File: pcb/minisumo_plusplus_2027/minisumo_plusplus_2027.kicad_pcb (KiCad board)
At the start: 2 copper layers, 211.1 x 112.8 mm, 9 parts, among them J3 Start Module - Conn_01x04_Pin, J5 Conn_01x10_Pin, SW1 SW_SPDT, U3 ESP32-C6-SuperMini

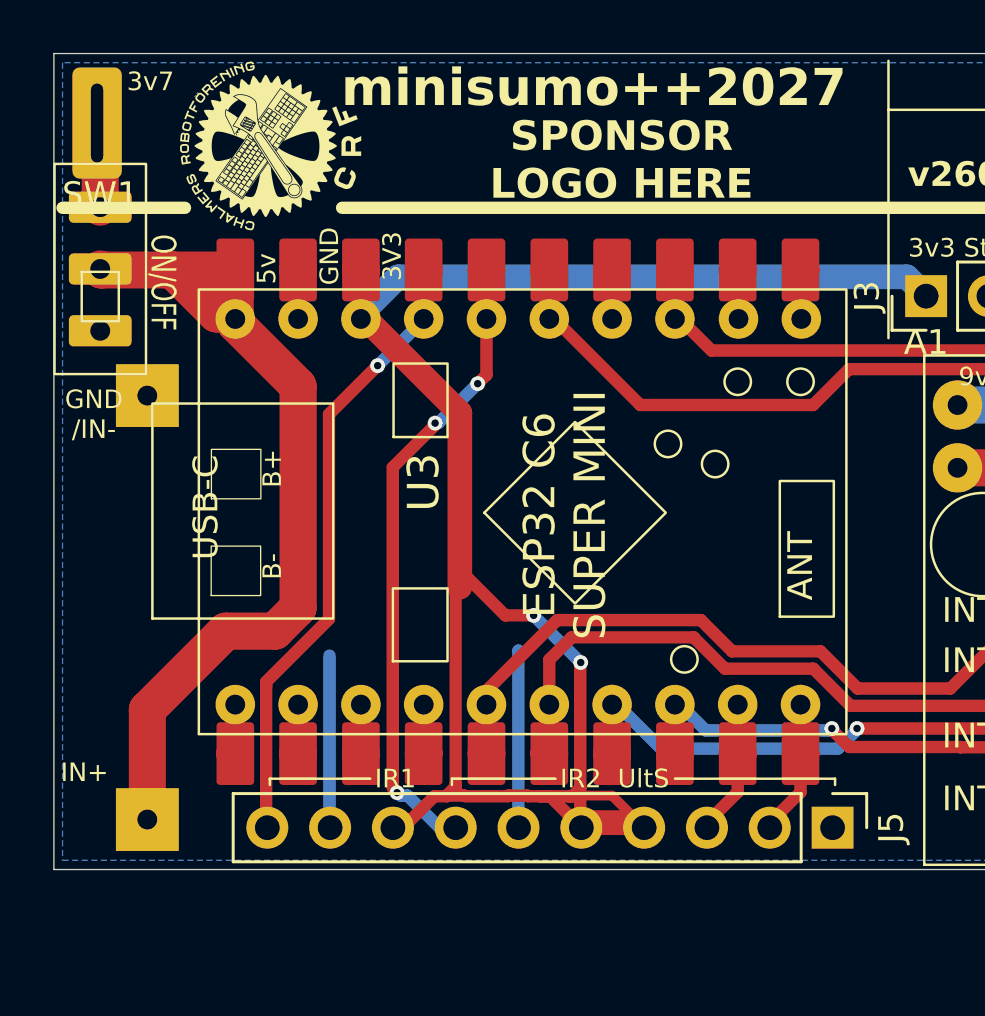
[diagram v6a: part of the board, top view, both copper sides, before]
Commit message: pcb refreshed ground plane
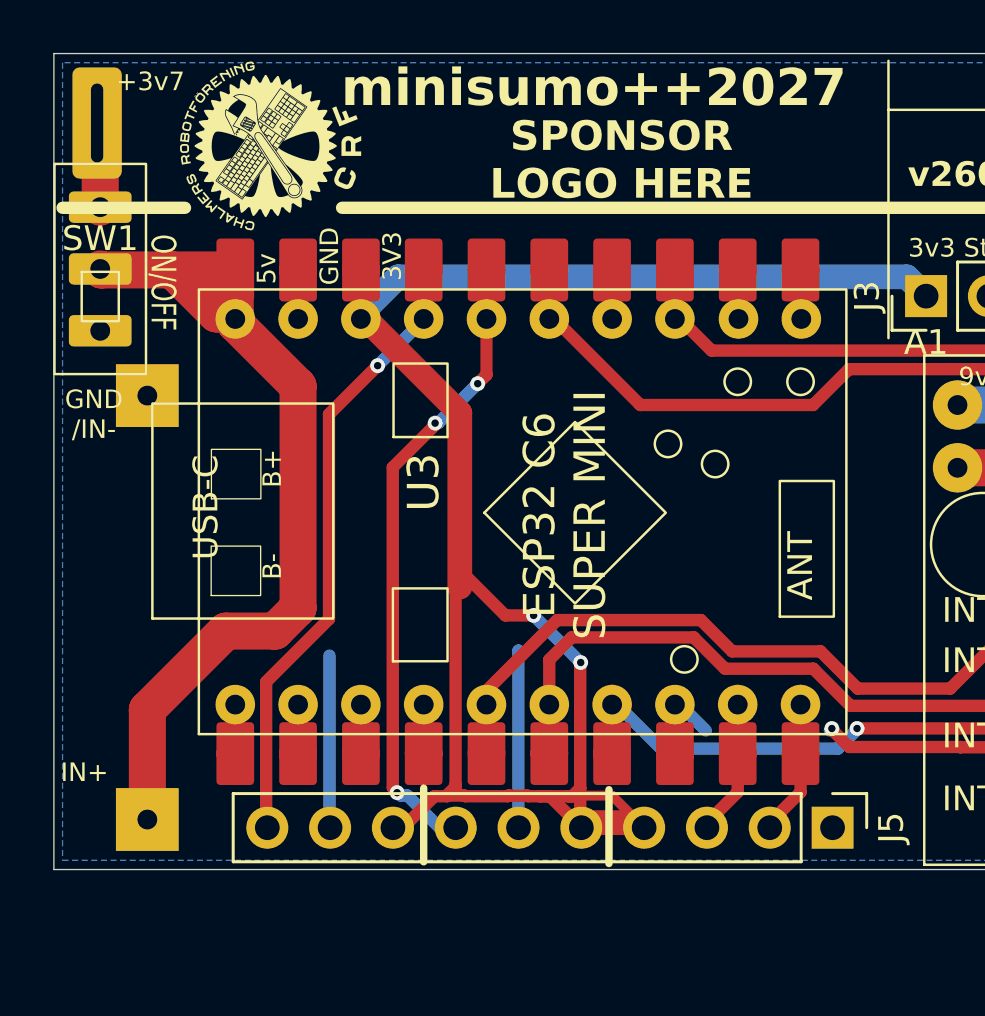
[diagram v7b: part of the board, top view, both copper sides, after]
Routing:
- net Net-(A1-INT4): track 18.6 -> 13.5 mm
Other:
- board text added: "+3v7"
- board text added: "3v3"
- board text removed: "3v7"

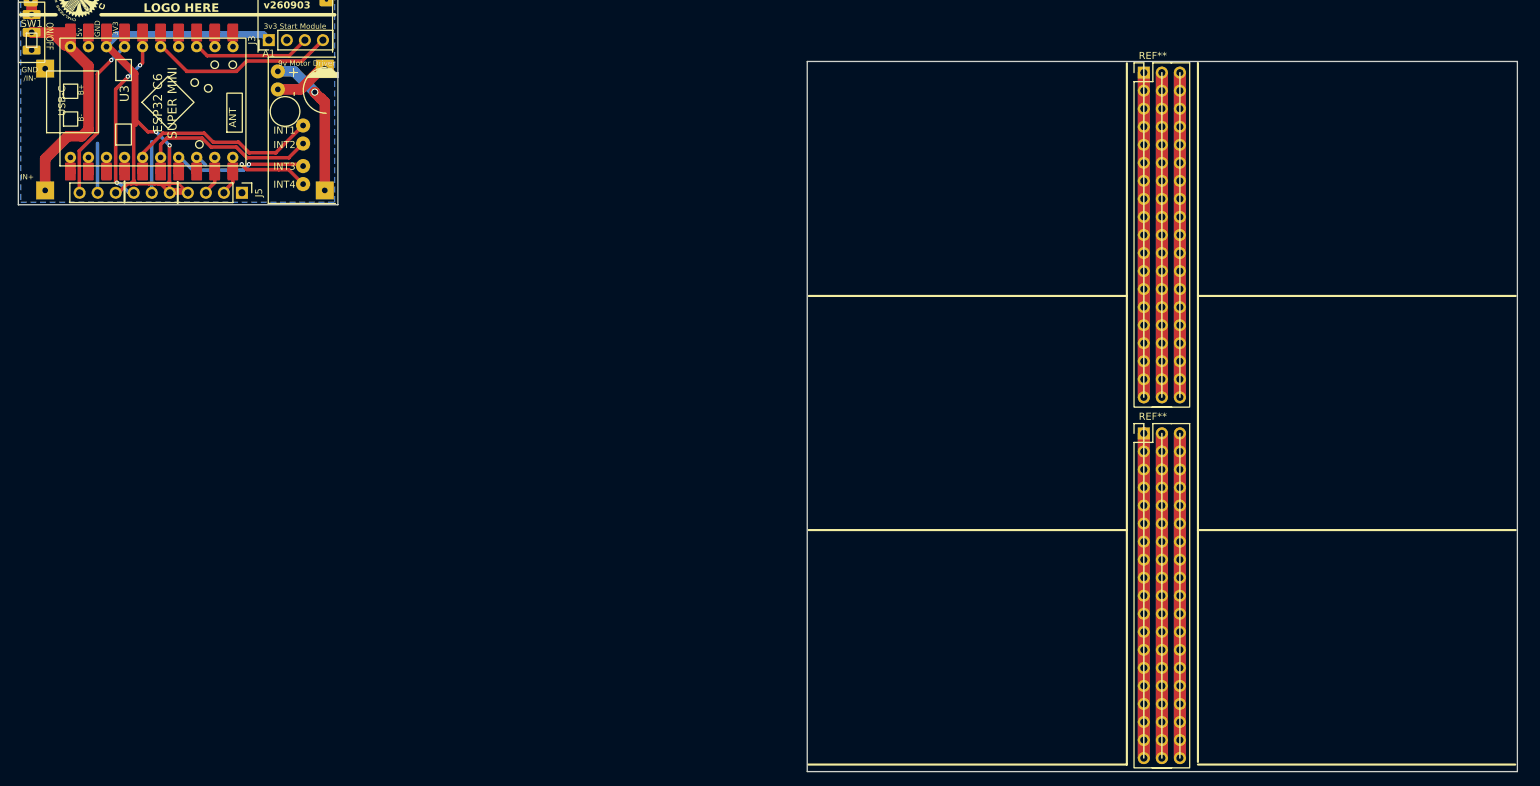
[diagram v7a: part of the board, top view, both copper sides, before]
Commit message: pcb latest w/ clean cutout and gerber (6x in 10x10cm)
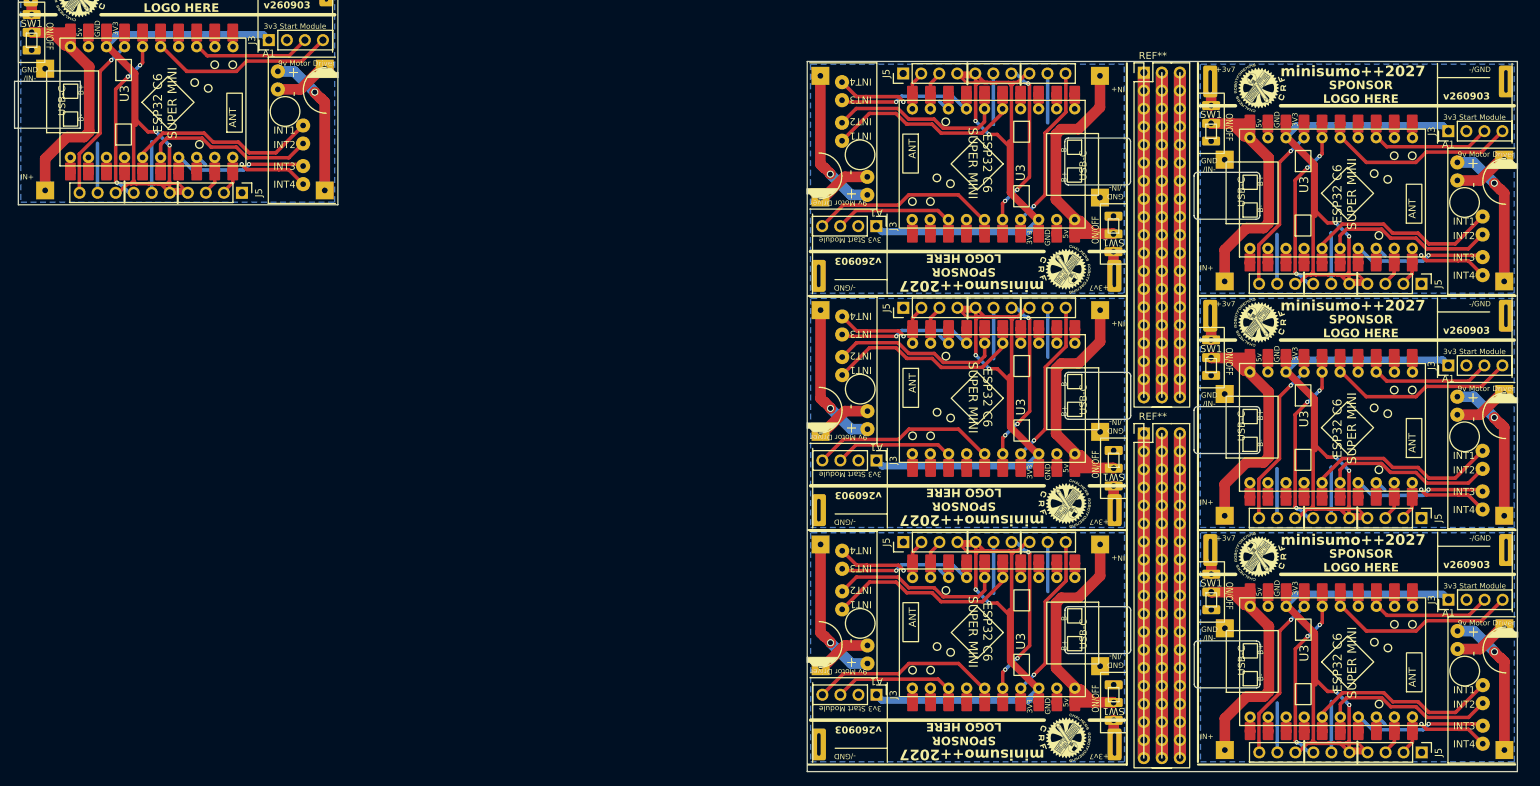
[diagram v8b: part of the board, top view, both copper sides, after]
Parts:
- added A1: ~, minisumo_plusplus_2027:Mini_L298N_2_Channel_H_Bridge_DC_Motor_Driver_Board_with_MX1508-special_silk, F.Cu at (149.7, 101.8)
- added A1: ~, minisumo_plusplus_2027:Mini_L298N_2_Channel_H_Bridge_DC_Motor_Driver_Board_with_MX1508-special_silk, F.Cu at (230.3, 126.2)
- added A1: ~, minisumo_plusplus_2027:Mini_L298N_2_Channel_H_Bridge_DC_Motor_Driver_Board_with_MX1508-special_silk, F.Cu at (230.2, 93.2)
- added A1: ~, minisumo_plusplus_2027:Mini_L298N_2_Channel_H_Bridge_DC_Motor_Driver_Board_with_MX1508-special_silk, F.Cu at (149.7, 68.8)
- added A1: ~, minisumo_plusplus_2027:Mini_L298N_2_Channel_H_Bridge_DC_Motor_Driver_Board_with_MX1508-special_silk, F.Cu at (230.2, 60.2)
- added A1: ~, minisumo_plusplus_2027:Mini_L298N_2_Channel_H_Bridge_DC_Motor_Driver_Board_with_MX1508-special_silk, F.Cu at (149.7, 134.8)
- added A2: ~, minisumo_plusplus_2027:XL6009 4A Boost Converter Step Up Adjustable 15W 5-32V to 5-50V DC-DC Power Supply Module LM2577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, B.Cu at (183.1, 114.1)
- added A2: ~, minisumo_plusplus_2027:XL6009 4A Boost Converter Step Up Adjustable 15W 5-32V to 5-50V DC-DC Power Supply Module LM2577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, B.Cu at (183.1, 48.1)
- added A2: ~, minisumo_plusplus_2027:XL6009 4A Boost Converter Step Up Adjustable 15W 5-32V to 5-50V DC-DC Power Supply Module LM2577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, B.Cu at (196.8, 80.9)
- added A2: ~, minisumo_plusplus_2027:XL6009 4A Boost Converter Step Up Adjustable 15W 5-32V to 5-50V DC-DC Power Supply Module LM2577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, B.Cu at (196.9, 146.9)
- added A2: ~, minisumo_plusplus_2027:XL6009 4A Boost Converter Step Up Adjustable 15W 5-32V to 5-50V DC-DC Power Supply Module LM2577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, B.Cu at (183.1, 81.1)
- added A2: ~, minisumo_plusplus_2027:XL6009 4A Boost Converter Step Up Adjustable 15W 5-32V to 5-50V DC-DC Power Supply Module LM2577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, B.Cu at (196.8, 113.9)
- added J3: Start Module - Conn_01x04_Pin, Connector_PinHeader_2.54mm:PinHeader_1x04_P2.54mm_Vertical, F.Cu at (230.3, 123.8)
- added J3: Start Module - Conn_01x04_Pin, Connector_PinHeader_2.54mm:PinHeader_1x04_P2.54mm_Vertical, F.Cu at (149.7, 137.2)
- added J3: Start Module - Conn_01x04_Pin, Connector_PinHeader_2.54mm:PinHeader_1x04_P2.54mm_Vertical, F.Cu at (230.2, 57.8)
- added J3: Start Module - Conn_01x04_Pin, Connector_PinHeader_2.54mm:PinHeader_1x04_P2.54mm_Vertical, F.Cu at (149.7, 71.2)
- added J3: Start Module - Conn_01x04_Pin, Connector_PinHeader_2.54mm:PinHeader_1x04_P2.54mm_Vertical, F.Cu at (149.7, 104.2)
- added J3: Start Module - Conn_01x04_Pin, Connector_PinHeader_2.54mm:PinHeader_1x04_P2.54mm_Vertical, F.Cu at (230.2, 90.8)
- added J5: Conn_01x10_Pin, Connector_PinHeader_2.54mm:PinHeader_1x10_P2.54mm_Vertical, F.Cu at (226.4, 112.3)
- added J5: Conn_01x10_Pin, Connector_PinHeader_2.54mm:PinHeader_1x10_P2.54mm_Vertical, F.Cu at (153.5, 82.7)
- added J5: Conn_01x10_Pin, Connector_PinHeader_2.54mm:PinHeader_1x10_P2.54mm_Vertical, F.Cu at (226.5, 145.3)
- added J5: Conn_01x10_Pin, Connector_PinHeader_2.54mm:PinHeader_1x10_P2.54mm_Vertical, F.Cu at (153.5, 115.7)
- added J5: Conn_01x10_Pin, Connector_PinHeader_2.54mm:PinHeader_1x10_P2.54mm_Vertical, F.Cu at (226.4, 79.3)
- added J5: Conn_01x10_Pin, Connector_PinHeader_2.54mm:PinHeader_1x10_P2.54mm_Vertical, F.Cu at (153.5, 49.7)
- added SW1: SW_SPDT, minisumo_plusplus_2027:SPST_switch_SS-12D00G4_1P2T_2.5mm_pitch_vert, F.Cu at (196.8, 87.2)
- added SW1: SW_SPDT, minisumo_plusplus_2027:SPST_switch_SS-12D00G4_1P2T_2.5mm_pitch_vert, F.Cu at (183.1, 74.8)
- added SW1: SW_SPDT, minisumo_plusplus_2027:SPST_switch_SS-12D00G4_1P2T_2.5mm_pitch_vert, F.Cu at (183.1, 140.8)
- added SW1: SW_SPDT, minisumo_plusplus_2027:SPST_switch_SS-12D00G4_1P2T_2.5mm_pitch_vert, F.Cu at (183.1, 107.8)
- added SW1: SW_SPDT, minisumo_plusplus_2027:SPST_switch_SS-12D00G4_1P2T_2.5mm_pitch_vert, F.Cu at (196.9, 120.2)
- added SW1: SW_SPDT, minisumo_plusplus_2027:SPST_switch_SS-12D00G4_1P2T_2.5mm_pitch_vert, F.Cu at (196.8, 54.2)
- added U2: ~, minisumo_plusplus_2027:battery cr123 3.7v with contacts for 18650_special_silk, B.Cu at (183.2, 144.2)
- added U2: ~, minisumo_plusplus_2027:battery cr123 3.7v with contacts for 18650_special_silk, B.Cu at (196.7, 50.8)
- added U2: ~, minisumo_plusplus_2027:battery cr123 3.7v with contacts for 18650_special_silk, B.Cu at (196.7, 83.8)
- added U2: ~, minisumo_plusplus_2027:battery cr123 3.7v with contacts for 18650_special_silk, B.Cu at (196.7, 116.8)
- added U2: ~, minisumo_plusplus_2027:battery cr123 3.7v with contacts for 18650_special_silk, B.Cu at (183.2, 78.2)
- added U2: ~, minisumo_plusplus_2027:battery cr123 3.7v with contacts for 18650_special_silk, B.Cu at (183.2, 111.2)
- added U3: ESP32-C6-SuperMini, minisumo_plusplus_2027:ESP32-C6-SuperMini_SMD_THT, F.Cu at (177.6, 137.3)
- added U3: ESP32-C6-SuperMini, minisumo_plusplus_2027:ESP32-C6-SuperMini_SMD_THT, F.Cu at (202.3, 57.7)
- added U3: ESP32-C6-SuperMini, minisumo_plusplus_2027:ESP32-C6-SuperMini_SMD_THT, F.Cu at (202.3, 123.7)
- added U3: ESP32-C6-SuperMini, minisumo_plusplus_2027:ESP32-C6-SuperMini_SMD_THT, F.Cu at (202.3, 90.7)
- added U3: ESP32-C6-SuperMini, minisumo_plusplus_2027:ESP32-C6-SuperMini_SMD_THT, F.Cu at (177.6, 104.3)
- added U3: ESP32-C6-SuperMini, minisumo_plusplus_2027:ESP32-C6-SuperMini_SMD_THT, F.Cu at (177.6, 71.3)
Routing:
- net 3v3: track 75.5 -> 528.6 mm, vias 2 -> 14
- net /3v7 (>3v3 & <5v): track 36.3 -> 256.1 mm
- net START Kill - not mandatory for sumo: track 28.4 -> 198.6 mm
- net IR Rear: track 28.3 -> 198.0 mm, vias 3 -> 21
- net Net-(A1-INT1): track 28.1 -> 196.9 mm
- net Net-(A1-INT2): track 25.8 -> 180.8 mm
- net IR Front: track 25.3 -> 177.1 mm, vias 1 -> 7
- net /9v: track 20.9 -> 146.2 mm, vias 1 -> 7
- net Net-(A1-INT3): track 20.6 -> 144.3 mm, vias 1 -> 7
- net START Start: track 18.9 -> 132.5 mm
- net GND: track 14.1 -> 98.7 mm
- net Net-(A1-INT4): track 13.5 -> 94.8 mm, vias 1 -> 7
- net Net-(A1-gnd): track 7.31 -> 51.2 mm
- net US Echo Tx: track 5.85 -> 40.9 mm
- net US Trigger Rx: track 5.85 -> 40.9 mm
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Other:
- board size 211.1 x 112.8 mm -> 211.6 x 112.8 mm
